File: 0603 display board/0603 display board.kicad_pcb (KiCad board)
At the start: 2 copper layers, 36.6 x 19.9 mm, 60 parts, among them J1 bottom, J2 top

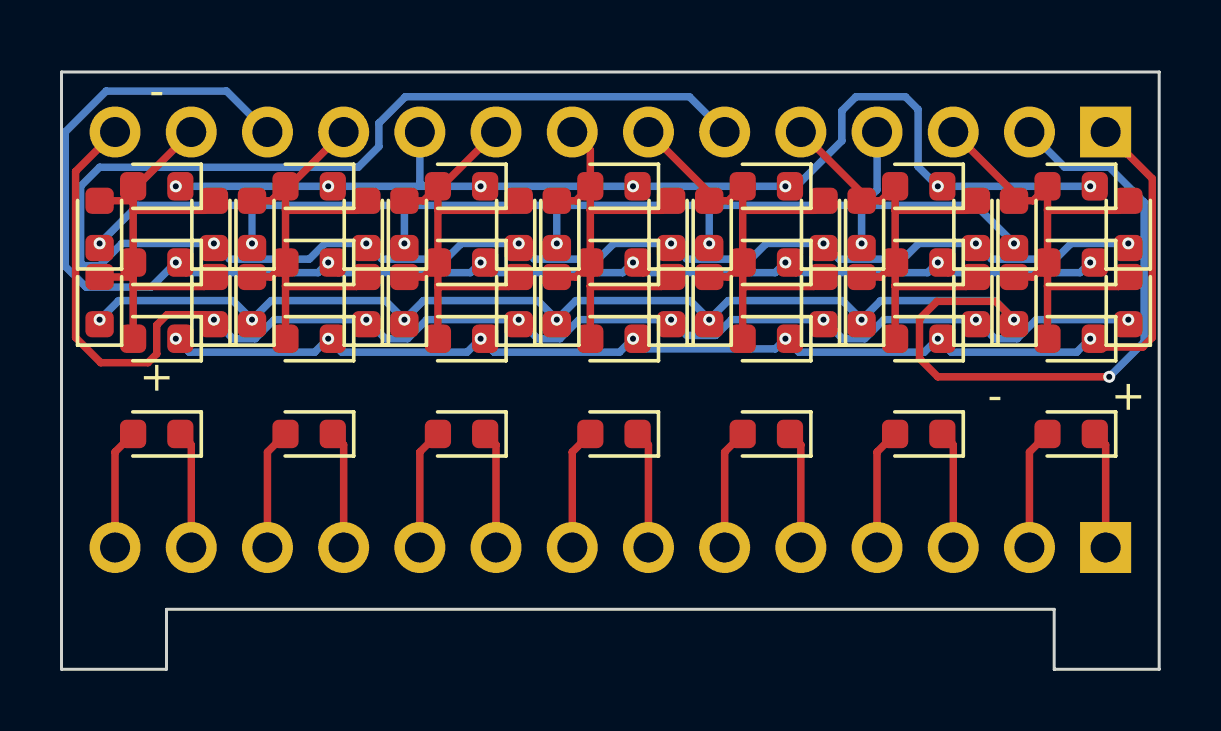
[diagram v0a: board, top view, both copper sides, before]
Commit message: smaller footprint
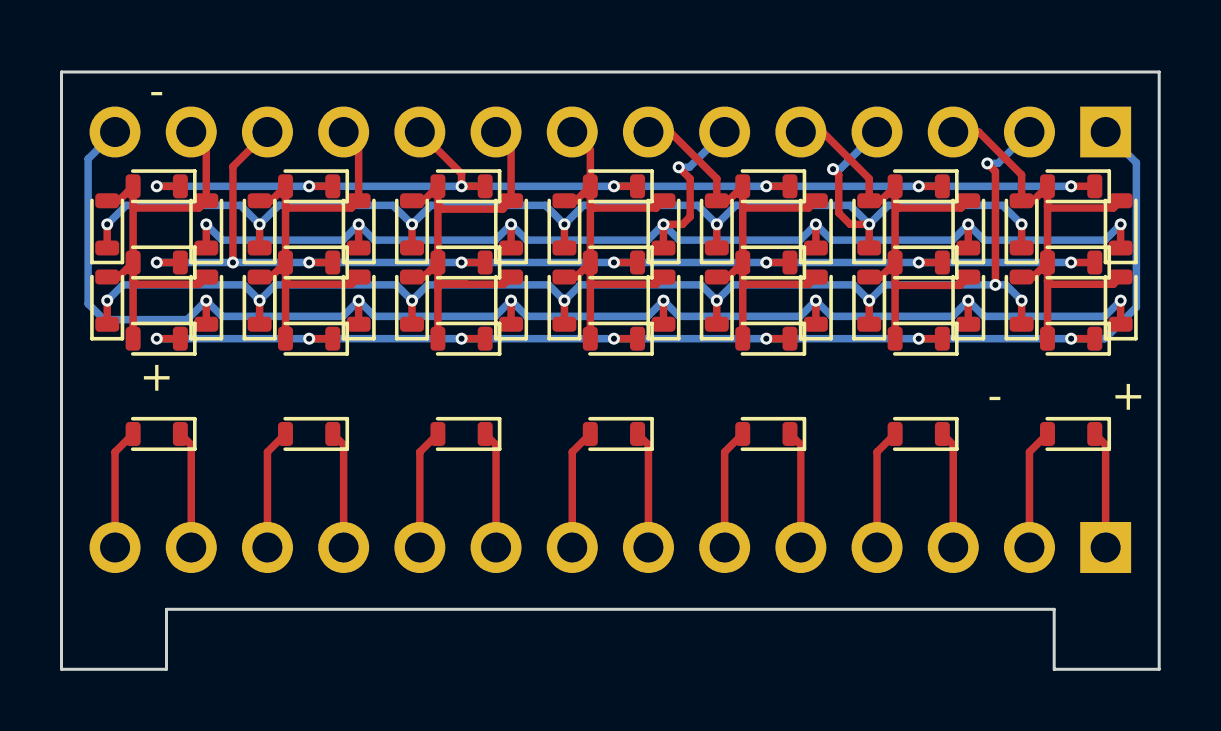
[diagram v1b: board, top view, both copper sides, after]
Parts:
- D1, D10, D11, D12, D13, D14, D15, D16, D17, D18, D19, D2, D20, D21, D22, D23, D24, D25, D26, D27, D28, D29, D3, D30, D31, D32, D33, D34, D35, D36, D37, D38, D39, D4, D40, D41, D42, D43, D44, D45, D46, D47, D48, D49, D5, D50, D51, D52, D53, D54, D55, D56, D6, D7, D8, D9: footprint LED_SMD:LED_0603_1608Metric -> Evan's misc parts:LED_0603_smallpads
- moved D1 0.25 mm to (133.6, 87.6)
- moved D2 0.25 mm to (133.6, 90.2)
- moved D20 0.25 mm to (142.0, 87.6)
- moved D21 0.25 mm to (142.0, 90.2)
- moved D27 0.25 mm to (143.8, 87.6)
- moved D28 0.25 mm to (143.8, 90.2)
- moved D48 0.25 mm to (152.1, 87.6)
- moved D49 0.25 mm to (152.1, 90.2)
- moved D50 0.25 mm to (153.9, 87.6)
- moved D51 0.25 mm to (153.9, 90.2)
- moved D13 0.25 mm to (162.3, 87.6)
- moved D14 0.25 mm to (162.3, 90.2)
- moved D15 0.25 mm to (138.7, 87.6)
- moved D16 0.25 mm to (138.7, 90.2)
- moved D22 0.25 mm to (164.1, 87.6)
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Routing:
- net B: track 64.1 -> 43.4 mm, vias 7 -> 8
- net E: track 56.3 -> 44.6 mm, vias 8 -> 9
- net G: track 48.8 -> 40.8 mm, vias 7 -> 8
- net F: track 40.5 -> 43.8 mm, vias 7 -> 8
- net D: track 42.4 -> 44.9 mm
- net C: track 47.3 -> 49.1 mm
- net A: track 36.7 -> 38.4 mm
- net Digit 2: track 16.1 -> 14.9 mm
- net Digit 4: track 15.4 -> 14.4 mm
- net Digit 1: track 15.7 -> 14.9 mm
- net Digit 5: track 16.5 -> 16.0 mm
